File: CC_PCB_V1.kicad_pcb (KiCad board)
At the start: 2 copper layers, 1 part, among them U2 level_converter_BOB-12009

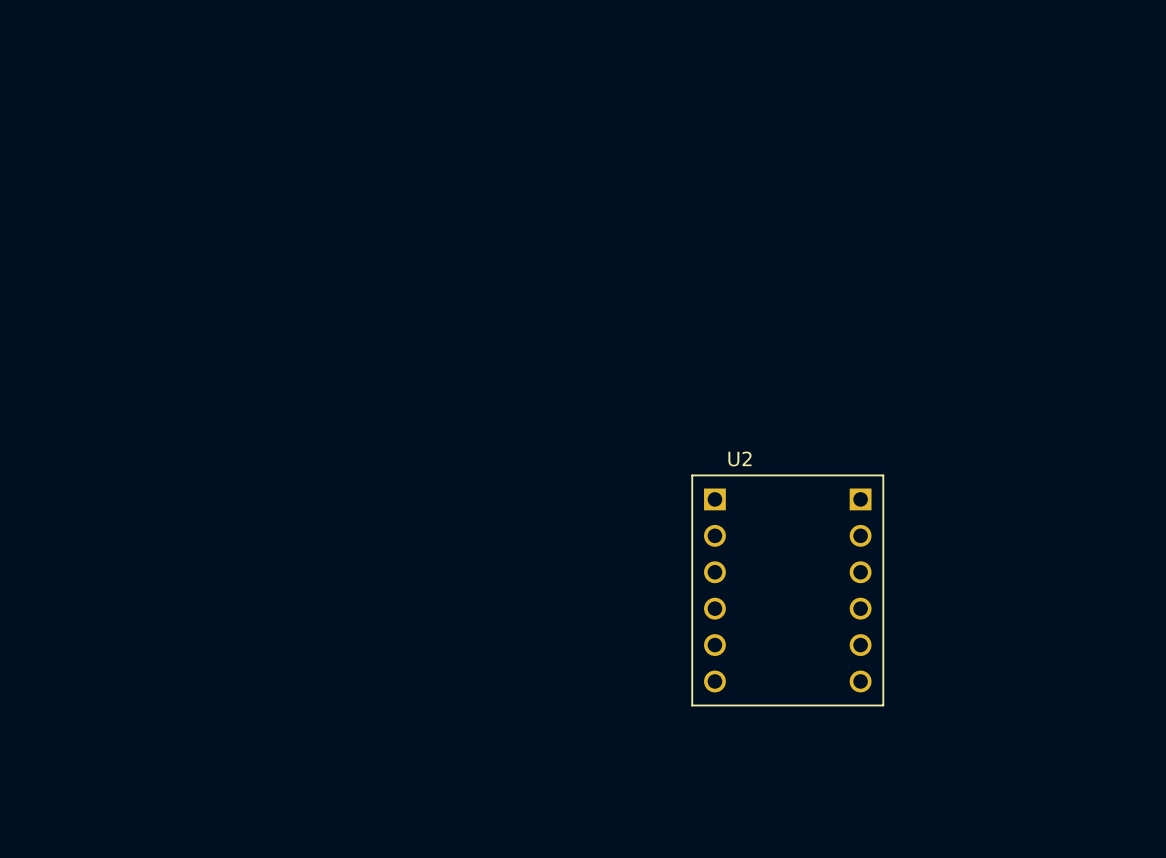
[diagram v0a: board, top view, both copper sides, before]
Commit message: Trying to fix 2 errors from DRC
Related to power > Lady Bug
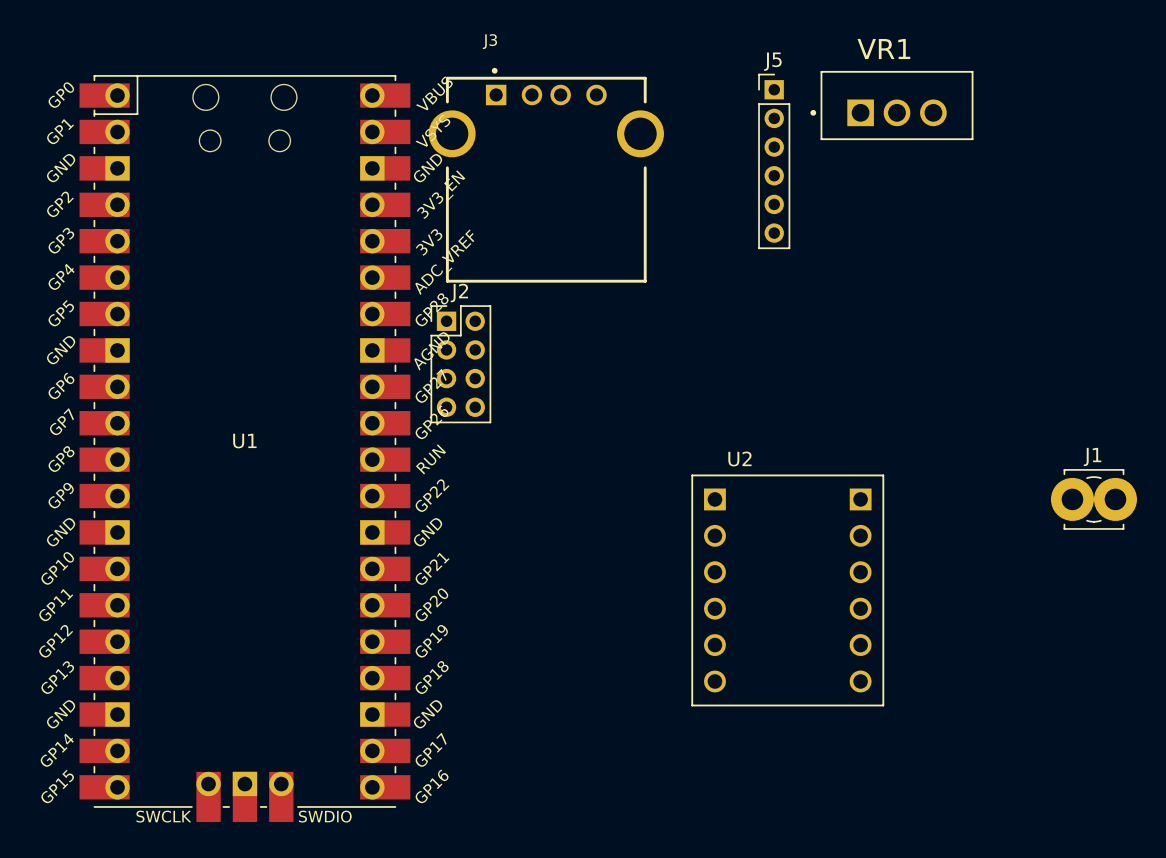
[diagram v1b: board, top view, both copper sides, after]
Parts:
- added J1: Screw_Terminal_01x02, TerminalBlock_MetzConnect:TerminalBlock_MetzConnect_360272_1x01_Horizontal_ScrewM2.6, F.Cu at (204.0, 61.0)
- added J2: Antenna_Conn_02x04_Odd_Even, Connector_PinHeader_2.00mm:PinHeader_2x04_P2.00mm_Vertical, F.Cu at (160.3, 48.5)
- added J3: USB1130-15-A_REVA, MCU_RaspberryPi_and_Boards:GCT_USB1130-15-A_REVA, F.Cu at (167.3, 35.5)
- added J5: Relay_Conn_01x06, Connector_PinHeader_2.00mm:PinHeader_1x06_P2.00mm_Vertical, F.Cu at (183.2, 32.4)
- added U1: Pico, MCU_RaspberryPi_and_Boards:RPi_Pico_SMD_TH, F.Cu at (146.3, 56.9)
- added VR1: LM1117T-3.3_NOPB, MCU_RaspberryPi_and_Boards:TO254P1054X470X1955-3, F.Cu at (191.8, 34.0)

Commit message: Wiring Board
I tried my best here,  let me know what you think.
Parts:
- moved J1 135.1 mm to (71.1, 36.8), turned to 270 degrees
- moved VR1 81.3 mm to (110.5, 36.8), turned to 270 degrees
- moved J5 80.1 mm to (110.5, 66.0)
- moved J3 76.1 mm to (91.2, 35.6), turned to 180 degrees
- moved J2 69.4 mm to (134.6, 113.0), turned to 90 degrees
- moved U2 54.0 mm to (135.9, 91.4), turned to 90 degrees
- moved U1 11.0 mm to (137.2, 50.8)
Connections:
- J1 pad 1: Net-(J1-Pad1) -> GND
- U2 pad GND_1: Net-(J1-Pad2) -> GND
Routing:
- net GND: track 0.00 -> 224.0 mm
- net +3V3: track 0.00 -> 150.6 mm
- net GP6: track 0.00 -> 91.0 mm
- net GP4: track 0.00 -> 90.1 mm
- net GP7: track 0.00 -> 87.0 mm
- net Net-(J1-Pad1): track 0.00 -> 83.5 mm
- net GP28: track 0.00 -> 72.1 mm
- net GP14: track 0.00 -> 70.4 mm
- net GP17: track 0.00 -> 53.4 mm
- net +5V: track 0.00 -> 51.0 mm
- net GP15: track 0.00 -> 48.4 mm
- net GP16: track 0.00 -> 39.0 mm
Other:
- board text added: "Autonomous Crazy Cart"
- board text added: "Design by: Dylan Ballback"

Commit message: Updated Screw Terminal Block
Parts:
- removed J1: Screw_Terminal_01x02, TerminalBlock_MetzConnect:TerminalBlock_MetzConnect_360272_1x01_Horizontal_ScrewM2.6
- added Screw_Terminal1: 282837-2, MCU_RaspberryPi_and_Boards:TE_282837-2, F.Cu at (68.6, 38.1)
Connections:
- U2 pad GND_1: GND -> Net-(Screw_Terminal1-Pad2)
- U2 pad GND_2: Net-(J1-Pad2) -> Net-(Screw_Terminal1-Pad2)
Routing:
- net Net-(Screw_Terminal1-Pad2): track 0.00 -> 92.6 mm
- net GND: track 224.0 -> 135.9 mm
- net Net-(Screw_Terminal1-Pad1): track 83.5 -> 85.6 mm

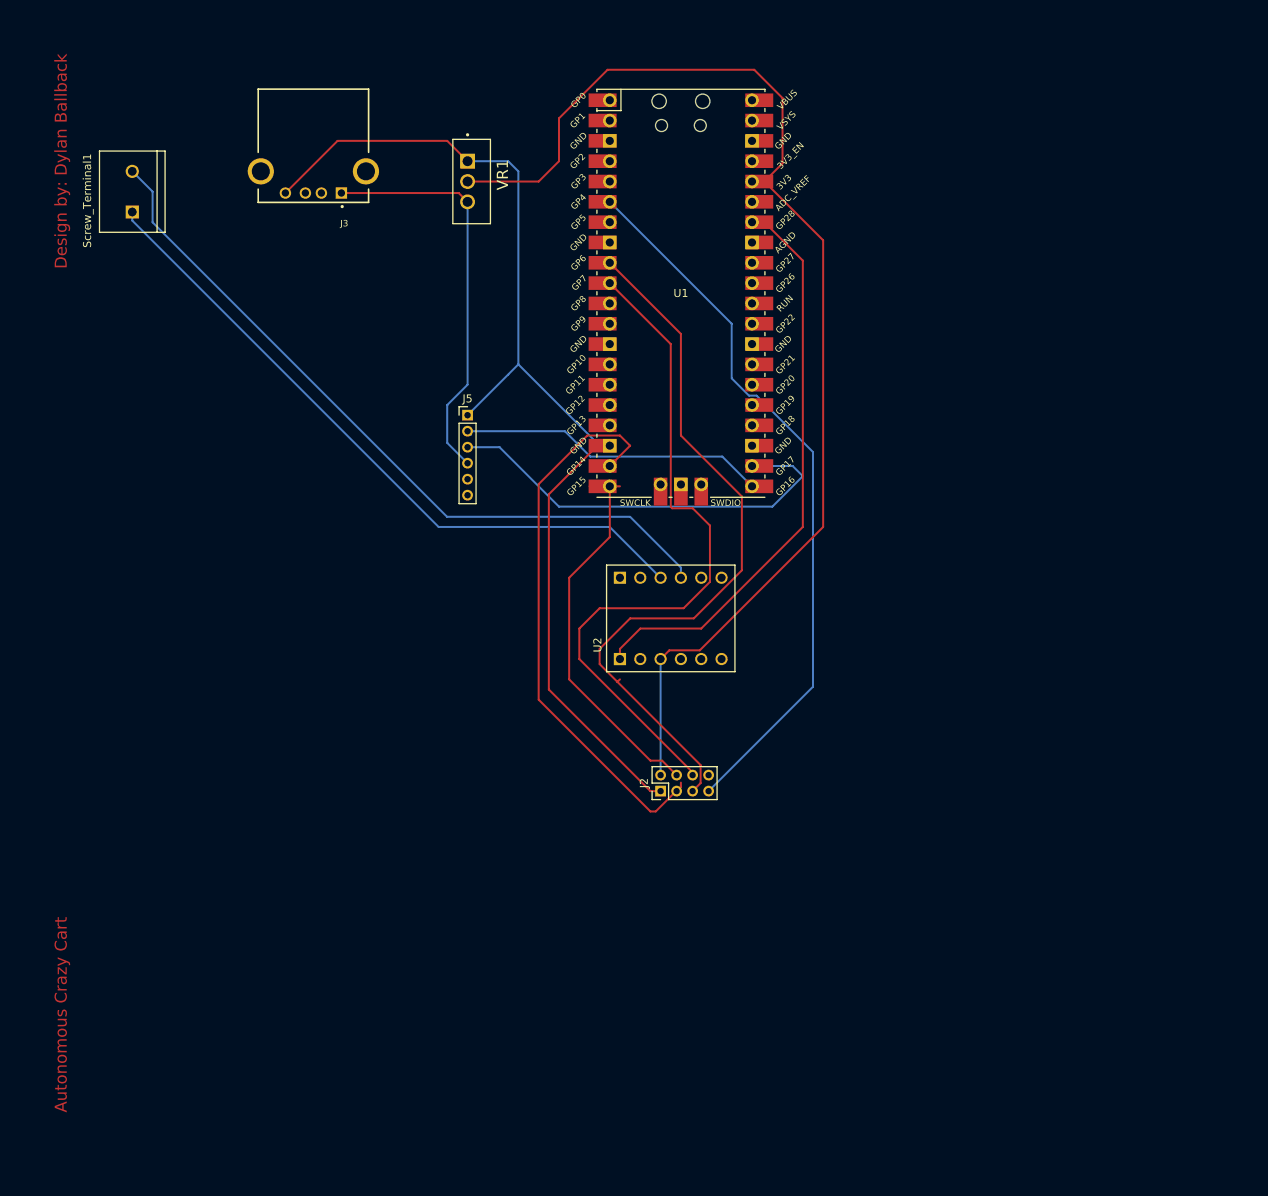
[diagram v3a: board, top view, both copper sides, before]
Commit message: Updated Circuit Wiring
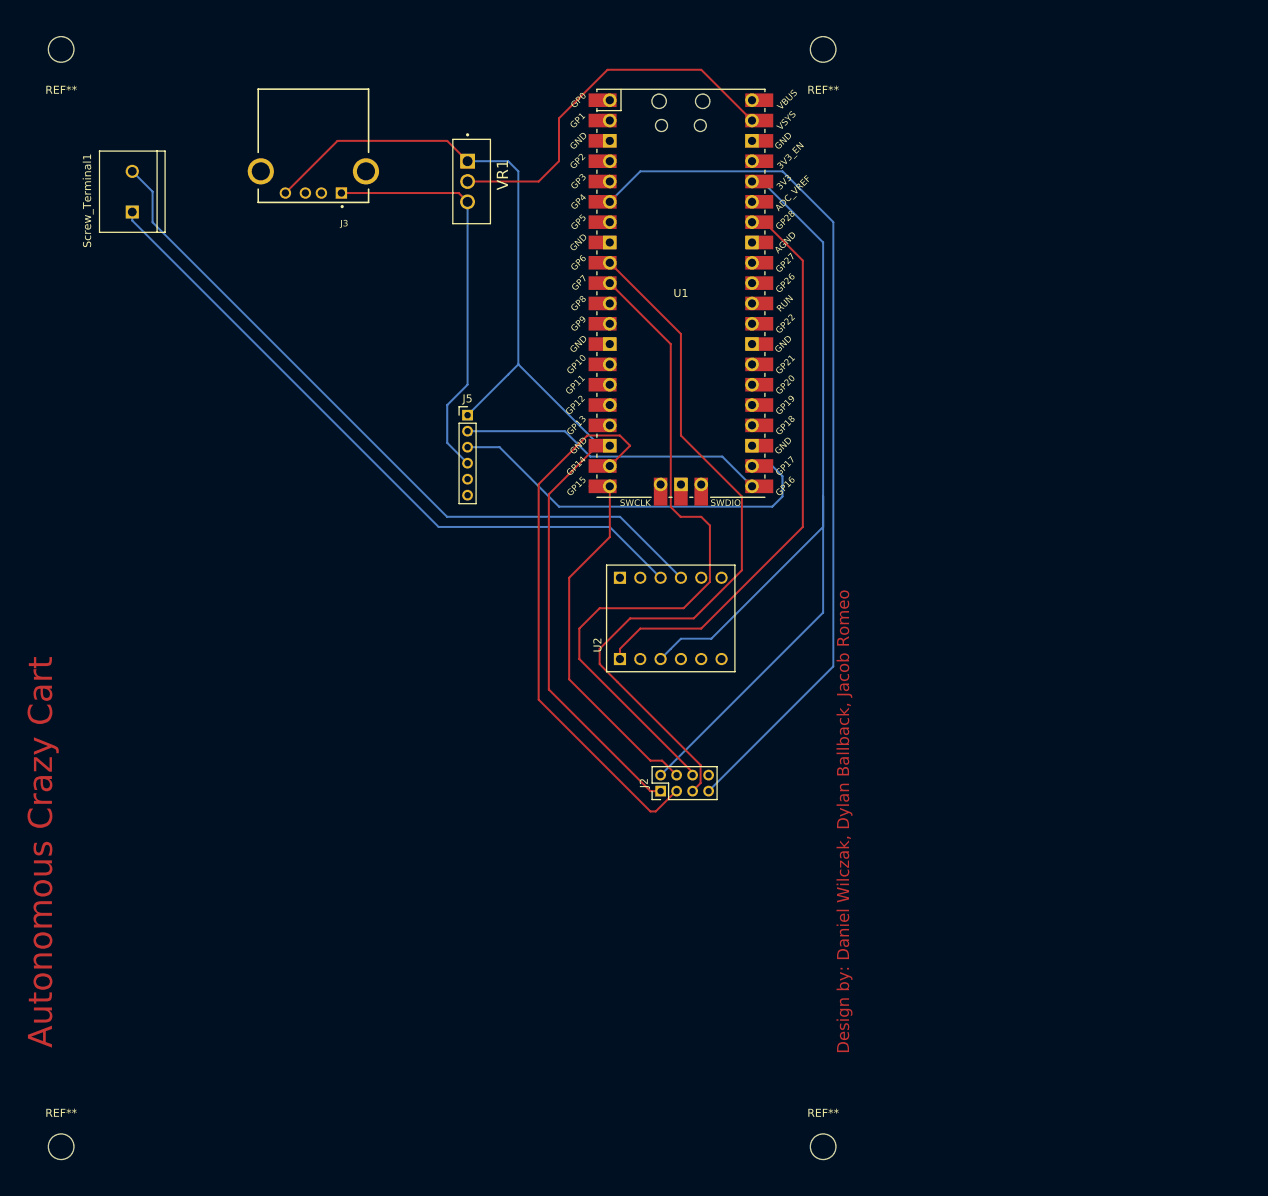
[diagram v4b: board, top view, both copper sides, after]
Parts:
- added REF**: MountingHole_3.2mm_M3, MountingHole:MountingHole_3.2mm_M3, F.Cu at (154.9, 20.3)
- added REF**: MountingHole_3.2mm_M3, MountingHole:MountingHole_3.2mm_M3, F.Cu at (59.7, 20.3)
- added REF**: MountingHole_3.2mm_M3, MountingHole:MountingHole_3.2mm_M3, F.Cu at (154.9, 157.5)
- added REF**: MountingHole_3.2mm_M3, MountingHole:MountingHole_3.2mm_M3, F.Cu at (59.7, 157.5)
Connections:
- U1 pad 39: Net-(U1-Pad39) -> +3V3
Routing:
- net GP4: track 90.1 -> 109.7 mm
- net +3V3: track 150.6 -> 166.7 mm
- net GP17: track 53.4 -> 49.8 mm
- net GP14: track 70.4 -> 69.1 mm
- net GP15: track 48.4 -> 47.2 mm
- net Net-(Screw_Terminal1-Pad2): track 92.6 -> 91.9 mm
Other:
- board text added: "Design by: Daniel Wilczak, Dylan Ballback, Jacob Romeo"
- board text removed: "Design by: Dylan Ballback"

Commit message: Completed V1 PCB
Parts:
- removed the REF** at (154.9, 20.3)
- removed the REF** at (59.7, 20.3)
- removed the REF** at (154.9, 157.5)
- removed the REF** at (59.7, 157.5)
- removed VR1: LM1117T-3.3_NOPB, MCU_RaspberryPi_and_Boards:TO254P1054X470X1955-3
- added REF**: MountingHole_3mm, MountingHole:MountingHole_3mm, F.Cu at (152.9, 155.4)
- added REF**: MountingHole_3mm, MountingHole:MountingHole_3mm, F.Cu at (60.5, 155.4)
- added REF**: MountingHole_3mm, MountingHole:MountingHole_3mm, F.Cu at (152.8, 22.3)
- added REF**: MountingHole_3mm, MountingHole:MountingHole_3mm, F.Cu at (60.6, 22.4)
- U2: footprint BOB-12009:CONV_BOB-12009 -> MCU_RaspberryPi_and_Boards:CONV_BOB-12009
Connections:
- J2 pad 2: +3V3 -> +5V
- Screw_Terminal1 pad 2: Net-(Screw_Terminal1-Pad2) -> GND
- U1 pad 36: +3V3 -> Net-(U1-Pad36)
- U1 pad 39: +3V3 -> +5V
- U2 pad GND_1: Net-(Screw_Terminal1-Pad2) -> GND
- U2 pad GND_2: Net-(Screw_Terminal1-Pad2) -> GND
- U2 pad LV: +3V3 -> +5V
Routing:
- net +3V3: track 166.7 -> 0.00 mm
- net +5V: track 51.0 -> 168.0 mm, vias 0 -> 1
- net GND: track 135.9 -> 22.3 mm, vias 0 -> 6
- net Net-(Screw_Terminal1-Pad2): track 91.9 -> 0.00 mm
- net GP14: track 69.1 -> 54.1 mm
- net GP7: track 87.0 -> 72.4 mm
- net Net-(J3-PadS1): track 0.00 -> 13.1 mm
- net GP4: track 109.7 -> 104.3 mm, vias 0 -> 1
- net Net-(U1-Pad36): track 0.00 -> 1.55 mm
- added copper zone on B.Cu, net GND
- added copper zone on F.Cu, net GND
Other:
- board outline added: 104.2 x 144.9 mm
- board text added: "Autonomous Crazy Cart V1"
- board text removed: "Autonomous Crazy Cart"

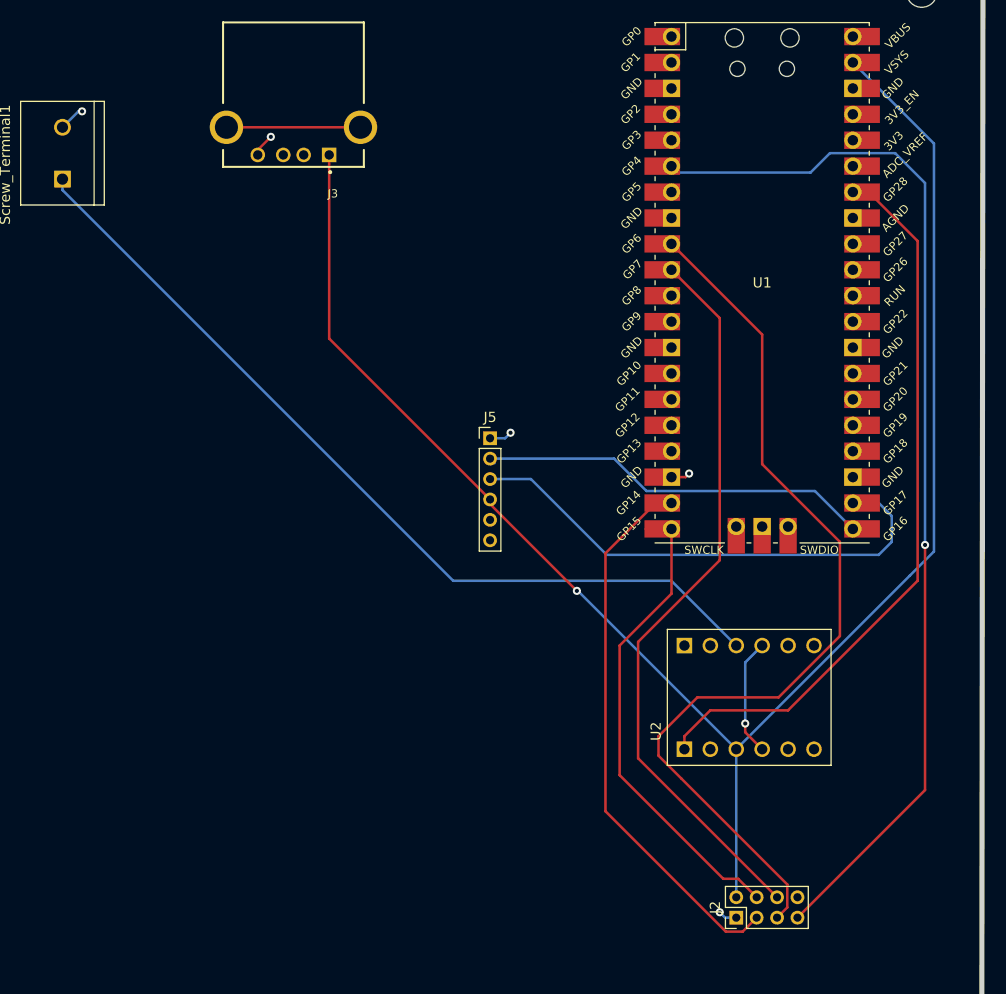
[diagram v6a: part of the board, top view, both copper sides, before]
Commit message: Finished SCH and added components to PCB
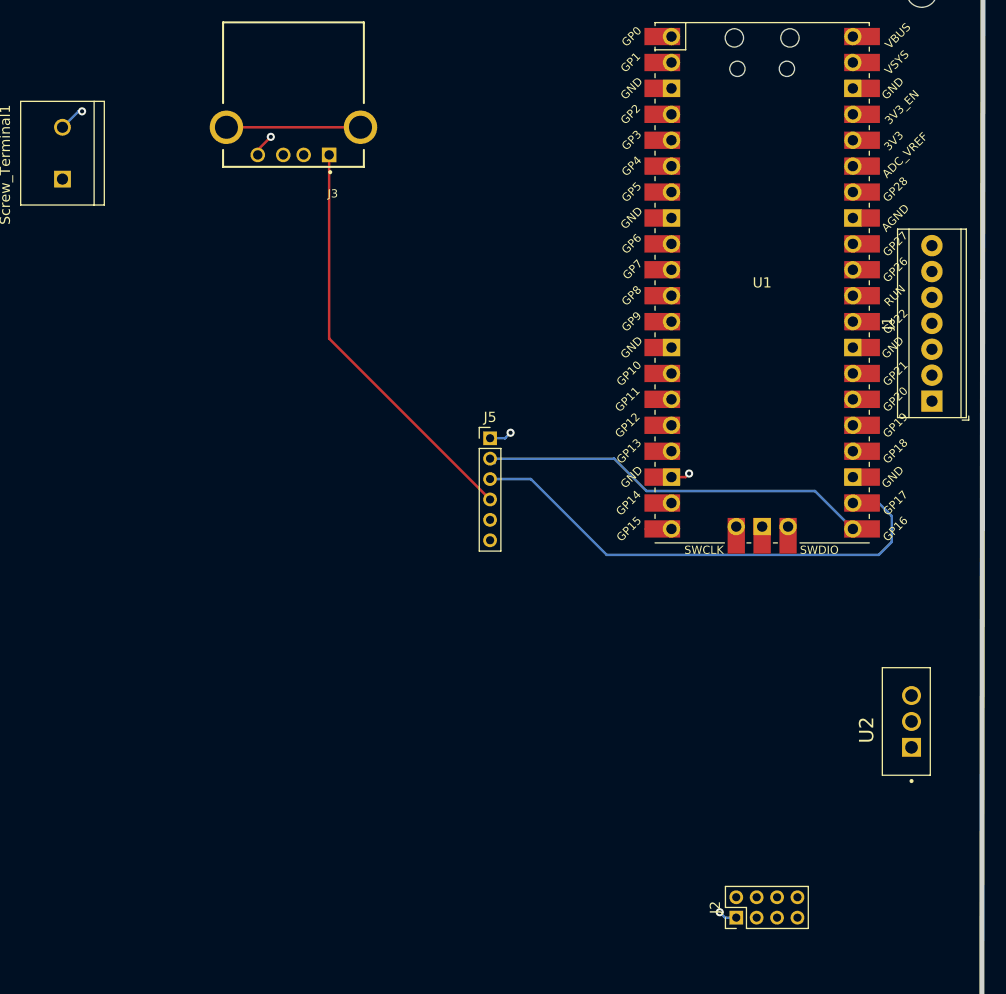
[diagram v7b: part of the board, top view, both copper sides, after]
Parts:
- added J1: Screw_Terminal_01x07, TerminalBlock_TE-Connectivity:TerminalBlock_TE_282834-7_1x07_P2.54mm_Horizontal, F.Cu at (153.8, 62.4)
- U2: value level_converter_BOB-12009 -> LM337_TO3; footprint MCU_RaspberryPi_and_Boards:CONV_BOB-12009 -> MCU_RaspberryPi_and_Boards:TO254P1054X470X1955-3
- moved U2 16.1 mm to (151.8, 93.8)
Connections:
- J2 pad 2: +5V -> +3.3V
- J2 pad 3: GP14 -> GP17
- J2 pad 4: GP15 -> GP14
- J2 pad 6: GP7 -> GP4
- J2 pad 7: GP4 -> GP7
- J5 pad 2: GP16 -> GP10
- J5 pad 3: GP17 -> GP11
- J5 pad 4: +5V -> Net-(J5-Pad4)
- J5 pad 6: Net-(J5-Pad6) -> +5V
- Screw_Terminal1 pad 1: Net-(Screw_Terminal1-Pad1) -> +5V
- U1 pad 16: Net-(U1-Pad16) -> GP12
- U1 pad 17: Net-(U1-Pad17) -> GP13
- U1 pad 21: GP16 -> Net-(U1-Pad21)
- U1 pad 22: GP17 -> Net-(U1-Pad22)
- U1 pad 27: Net-(U1-Pad27) -> GP21
- U1 pad 29: Net-(U1-Pad29) -> GP22
- U1 pad 31: Net-(U1-Pad31) -> GP26
- U1 pad 32: Net-(U1-Pad32) -> GP27
- U1 pad 36: Net-(U1-Pad36) -> 3.3V
- U1 pad 39: +5V -> +3.3V
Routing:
- net +5V: track 168.0 -> 40.3 mm, vias 1 -> 0
- net GP4: track 104.3 -> 0.00 mm, vias 1 -> 0
- net GP6: track 90.5 -> 0.00 mm
- net Net-(Screw_Terminal1-Pad1): track 85.6 -> 0.00 mm
- net GP7: track 72.4 -> 0.00 mm
- net GP28: track 72.1 -> 1.55 mm
- net GP14: track 54.1 -> 1.55 mm
- net GP15: track 47.2 -> 2.54 mm
- net GND: track 22.3 -> 10.8 mm, vias 6 -> 5
- net Net-(U1-Pad36): track 1.55 -> 0.00 mm
- net 3.3V: track 0.00 -> 1.55 mm

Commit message: "Finished" PCB
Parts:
- removed J3: USB1130-15-A_REVA, MCU_RaspberryPi_and_Boards:GCT_USB1130-15-A_REVA
- removed REF** (x4): MountingHole_3mm, MountingHole:MountingHole_3mm
- added C1: CP, Capacitor_THT:CP_Radial_D8.0mm_P5.00mm, F.Cu at (92.3, 26.7)
- added C2: C, Capacitor_THT:CP_Radial_D8.0mm_P5.00mm, F.Cu at (77.6, 37.2)
- U2: footprint MCU_RaspberryPi_and_Boards:TO254P1054X470X1955-3 -> MCU_RaspberryPi_and_Boards:SOT230P696X180-4N
- moved U2 82.4 mm to (91.3, 37.8), turned to 270 degrees
- moved J1 36.9 mm to (150.5, 99.2)
- moved Screw_Terminal1 5.43 mm to (64.7, 34.3)
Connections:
- net GP15 renamed Net-(U1-Pad20)
- U1 pad 14: Net-(U1-Pad14) -> GP10
- U1 pad 15: Net-(U1-Pad15) -> GP11
- U1 pad 22: Net-(U1-Pad22) -> GP17
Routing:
- net +3.3V: track 0.00 -> 167.0 mm
- net GP6: track 0.00 -> 86.0 mm, vias 0 -> 2
- net GP4: track 0.00 -> 78.1 mm, vias 0 -> 1
- net GP7: track 0.00 -> 74.3 mm, vias 0 -> 1
- net 3.3V: track 1.55 -> 68.5 mm
- net GP12: track 0.00 -> 45.2 mm, vias 0 -> 1
- net GP27: track 0.00 -> 43.9 mm
- net GP14: track 1.55 -> 43.6 mm
- net GP22: track 0.00 -> 40.5 mm
- net GP26: track 0.00 -> 40.4 mm
- net GP13: track 0.00 -> 40.2 mm
- net GP16: track 39.0 -> 0.00 mm
- net GP21: track 0.00 -> 36.8 mm, vias 0 -> 1
- net +5V: track 40.3 -> 75.7 mm
- net GP10: track 0.00 -> 21.9 mm
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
